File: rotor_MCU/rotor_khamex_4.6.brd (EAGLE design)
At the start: 156.5 x 131.8 mm, 45 parts, among them IC1 SN65HVD230DR, IC3 ELVX-L10D-HRRN-C-N2A4, J1 DF40C-80DS-0.4V(51)_ROWSWAP, J2 DF40C-80DS-0.4V(51)_ROWSWAP, J3 FTSH-110-01-F-DV, J4 612010235121, J5 612010235121, U1 LTC4368CMS-2#PBF

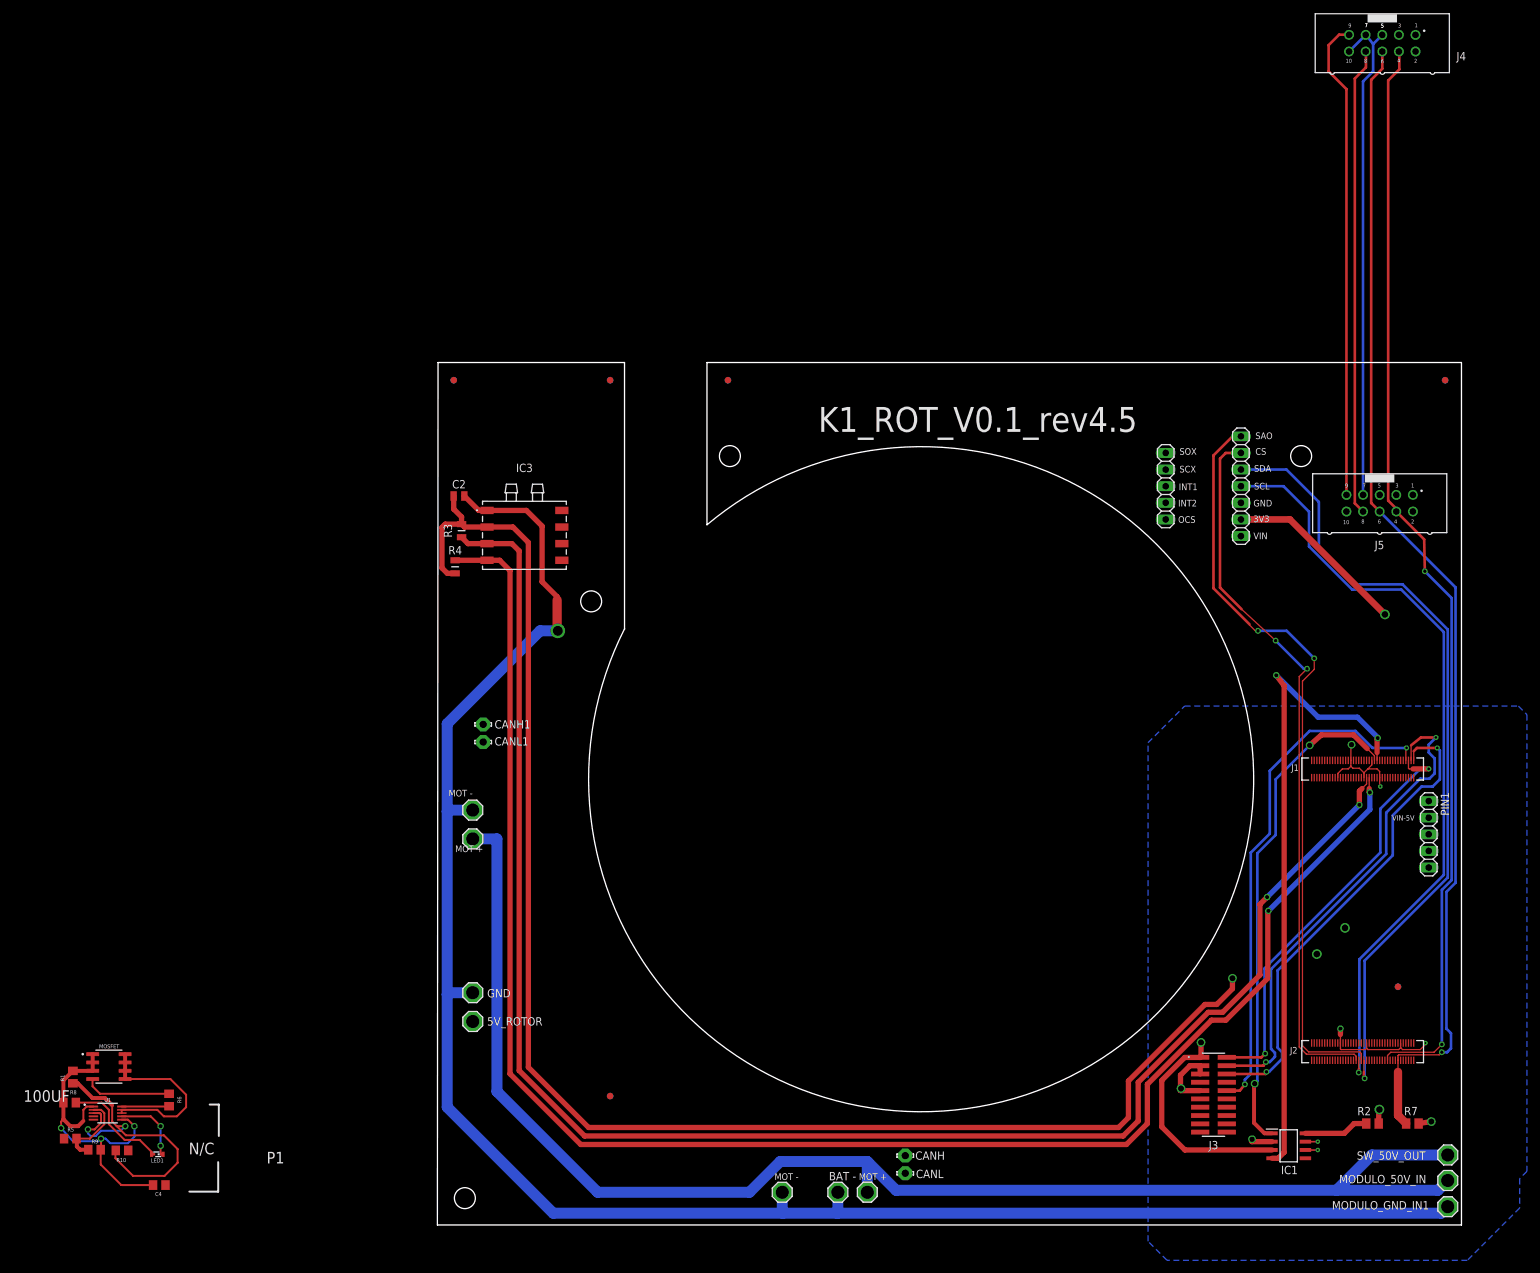
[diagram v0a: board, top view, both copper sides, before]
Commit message: JC: Cambios en zenit y rotor
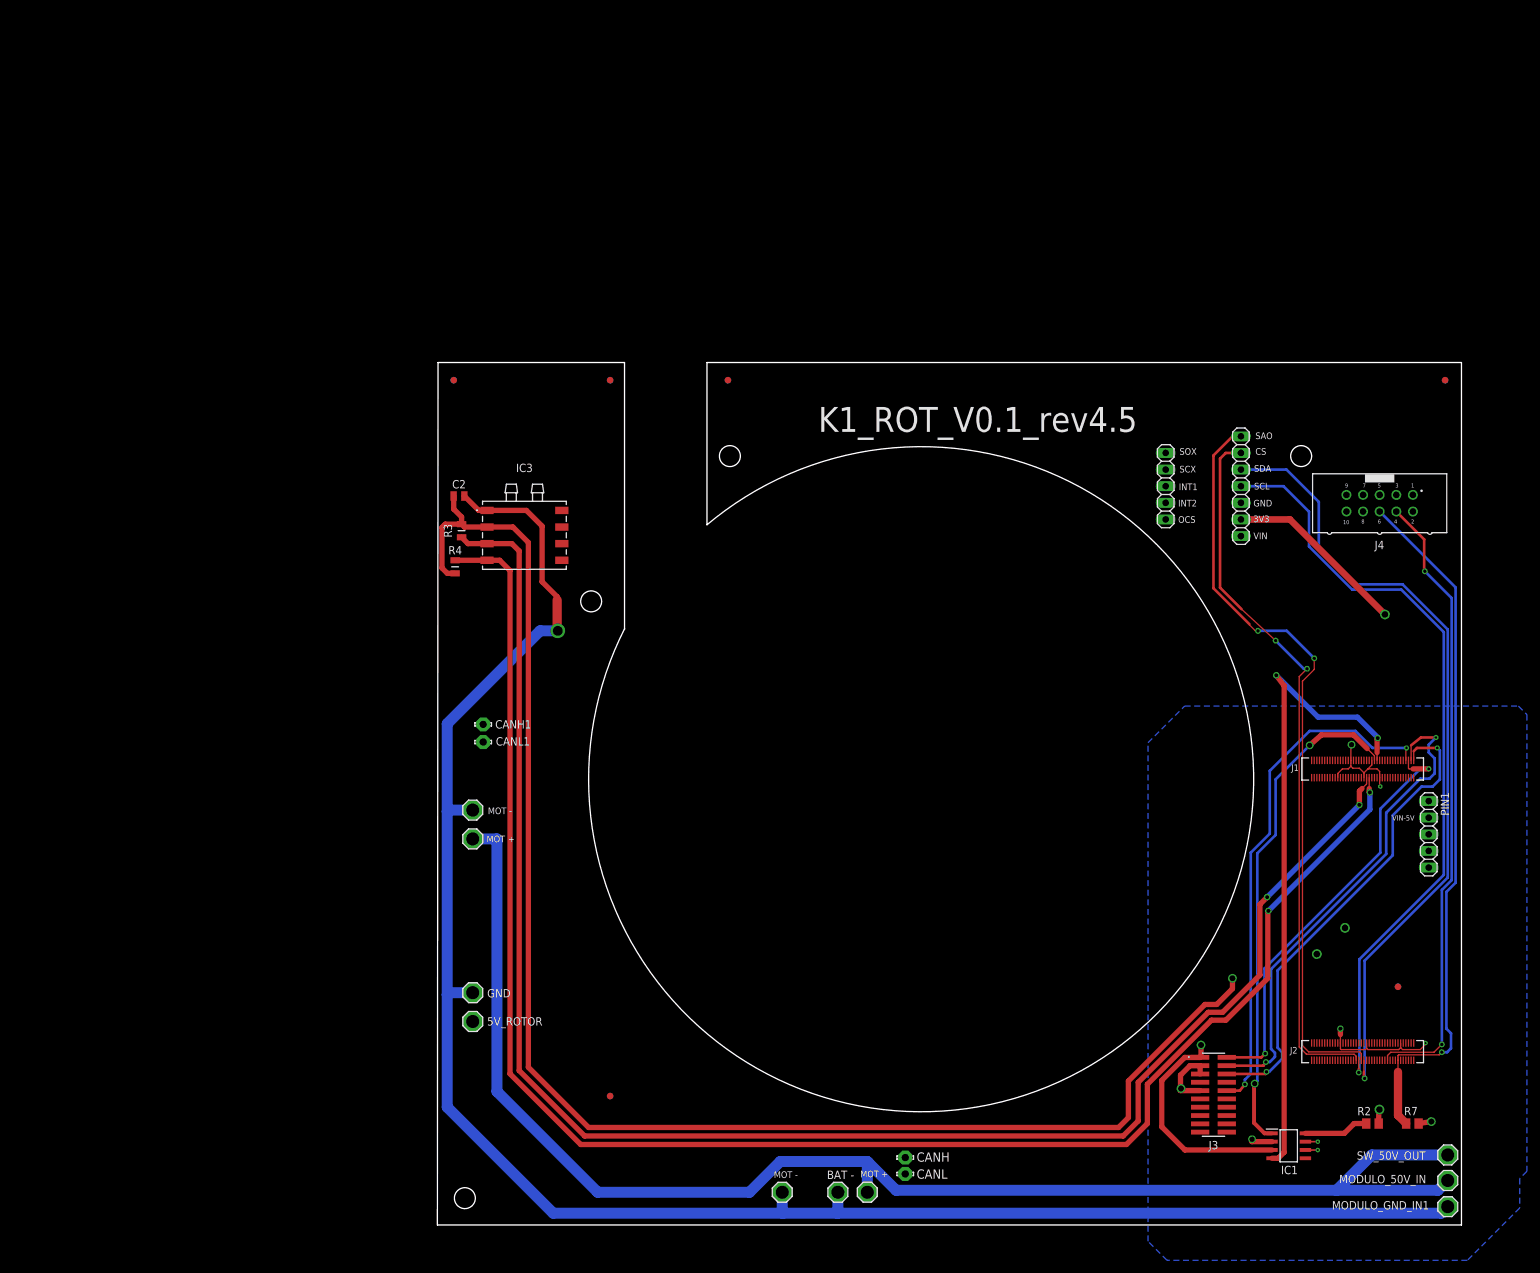
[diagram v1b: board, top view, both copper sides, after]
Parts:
- removed C4: 100nF, eagle-ltspice:C0805
- removed J5: 612010235121, Eagle_WR-BHD_rev24a:612010235121
- removed LED1: (no value), led:SMARTLED-TTW
- removed MOSFET: AO4407A, AO4407A:SOIC127P600X175-8N
- removed R1: 1.1M, eagle-ltspice:R0805
- removed R10, R5: 10k, eagle-ltspice:R0805
- removed R6: 100, eagle-ltspice:R0805
- removed R8: 22k, eagle-ltspice:R0805
- removed R9: 787k, eagle-ltspice:R0805
- removed U1: LTC4368CMS-2#PBF, LTC4368CMS-2_PBF:SOP50P490X110-10N
- moved J4 70.3 mm to (144.0, 110.3)
- moved CANH 0.30 mm to (71.5, 10.3)
- moved CANL 0.10 mm to (71.5, 7.80)
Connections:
- removed net GATE_PWR: MOSFET.4, R6.1
- removed net N$11: R5.2, R9.1, U1.2
- removed net N$12: R1.1, R10.2, U1.3
- removed net N$13: LED1.C@1, R8.2
- removed net N$14: R6.2, U1.10
- removed net N$2: LED1.A@1, U1.7
- removed net N$20: U1.4
- removed net N$21: U1.5
- removed net VBAT: MOSFET.5, MOSFET.6, MOSFET.7, MOSFET.8, U1.8, U1.9
- removed net VBAT_RAW: C4.2, MOSFET.1, MOSFET.2, MOSFET.3, R1.2, R8.1, R9.2, U1.1, U1.6
- net CANH: no longer J5.9
- net CANL: no longer J5.8
- net GND: no longer J5.10, J5.5, J5.7
- net PWM5: no longer J5.4
- net PWM9_SYNC: no longer J5.6
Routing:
- net GND: track 575.2 -> 499.2 mm
- net CANH: track 353.2 -> 280.2 mm
- net PWM9_SYNC: track 178.7 -> 107.2 mm
- net PWM5: track 166.8 -> 95.3 mm
- net CANL: track 348.9 -> 277.9 mm
- net VBAT_RAW: track 52.5 -> 0.00 mm, vias 3 -> 0
- net N$12: track 49.7 -> 0.00 mm, vias 2 -> 0
- net VBAT: track 27.4 -> 0.00 mm
- net N$13: track 16.5 -> 0.00 mm
- net GATE_PWR: track 13.3 -> 0.00 mm
- net N$11: track 11.9 -> 0.00 mm
- net N$2: track 10.9 -> 0.00 mm, vias 2 -> 0
- net N$14: track 7.26 -> 0.00 mm
- net 3V3-I2C: track 291.0 -> 285.8 mm
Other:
- board text removed: "100UF"
- board text removed: "FRONT"
- board text removed: "N/C"
- board text removed: "P1"
